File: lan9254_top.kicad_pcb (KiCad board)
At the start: 4 copper layers, 84 x 35 mm, 77 parts, among them J1 BEL_0845_2G1T_H5, SW1 SW_DIP_x08, U1 lan9254, U2 74LVC1G06, U3 74LVC1G06, U4 74LVC1G06, U5 PCA9306, U6 74LVC1G06, U8 24AA0x, X1 FNETHE025

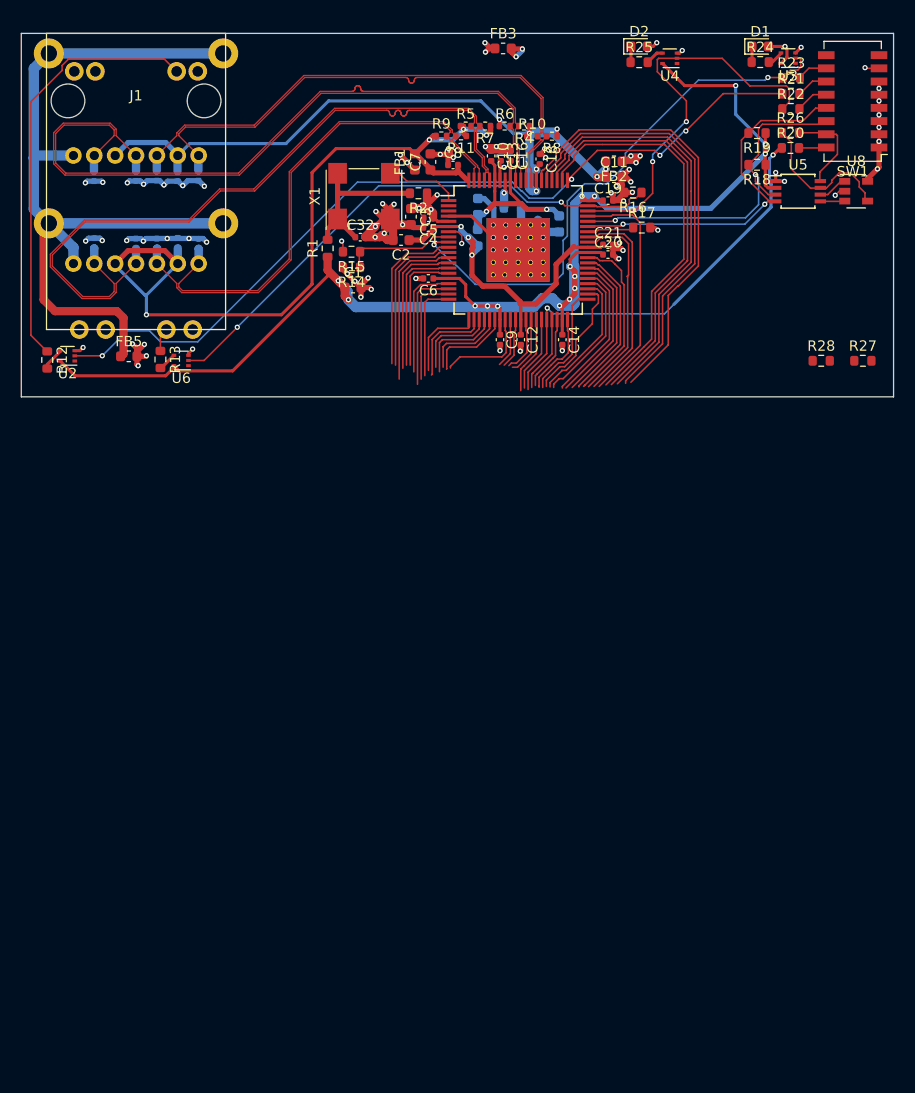
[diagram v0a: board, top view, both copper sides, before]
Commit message: added I/O connectors, JTAG (just in case) and more
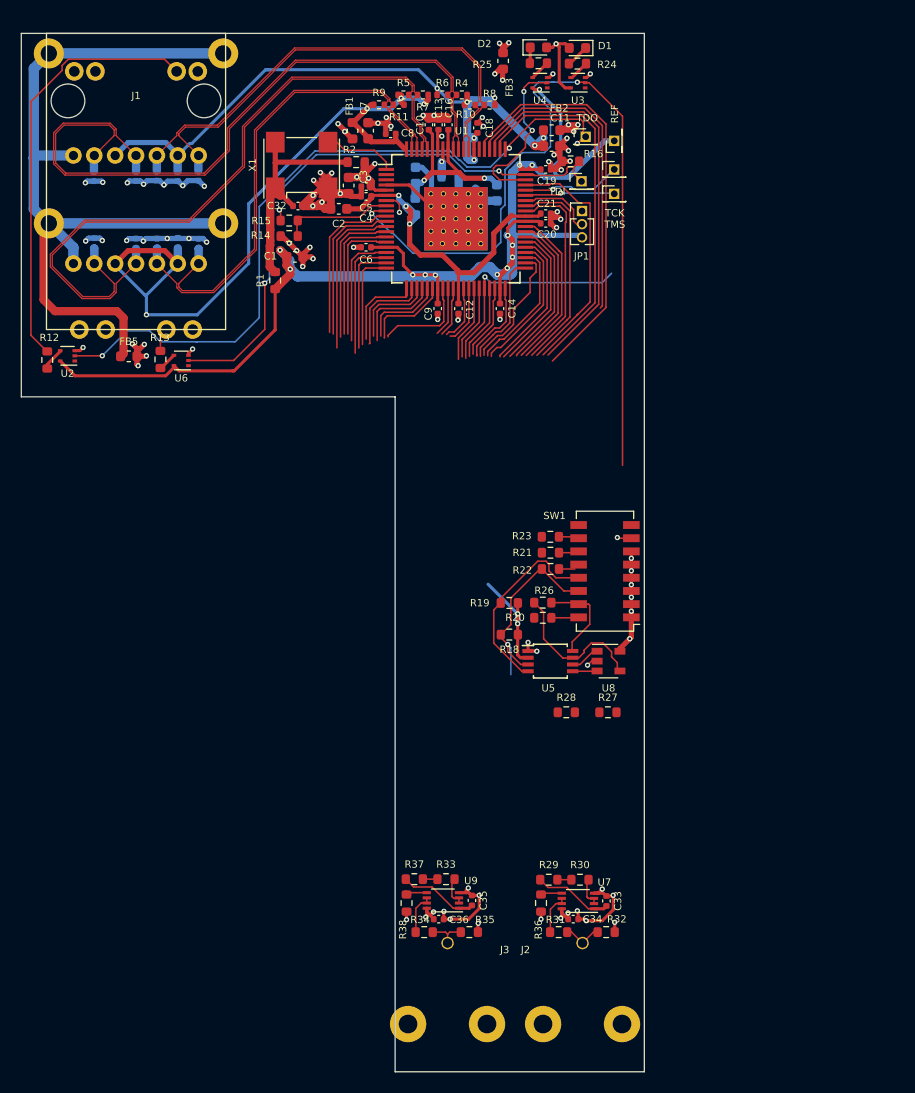
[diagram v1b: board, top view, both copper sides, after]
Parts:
- removed R17: 1k, Resistor_SMD:R_0603_1608Metric
- added C33: 100n, Capacitor_SMD:C_0402_1005Metric, F.Cu at (186.3, 123.5)
- added C34: 100n, Capacitor_SMD:C_0402_1005Metric, F.Cu at (183.2, 125.3)
- added C35: 100n, Capacitor_SMD:C_0402_1005Metric, F.Cu at (173.4, 123.5)
- added C36: 100n, Capacitor_SMD:C_0402_1005Metric, F.Cu at (170.2, 125.3)
- added J2: BNC, proj_footprints:BNC_Molex_0731713150, F.Cu at (184.1, 135.4)
- added J3: BNC, proj_footprints:BNC_Molex_0731713150, F.Cu at (171.1, 135.4)
- added JP1: Jumper_3_Bridged12, Connector_PinHeader_1.27mm:PinHeader_1x03_P1.27mm_Vertical, F.Cu at (184.0, 57.1)
- added R29: 100k, Resistor_SMD:R_0603_1608Metric, F.Cu at (180.8, 121.5)
- added R30: 100, Resistor_SMD:R_0603_1608Metric, F.Cu at (183.8, 121.5)
- added R31: 0, Resistor_SMD:R_0603_1608Metric, F.Cu at (181.8, 126.5)
- added R32: 100k, Resistor_SMD:R_0603_1608Metric, F.Cu at (186.3, 126.5)
- added R33: 100, Resistor_SMD:R_0603_1608Metric, F.Cu at (170.9, 121.5)
- added R34: 0, Resistor_SMD:R_0603_1608Metric, F.Cu at (168.8, 126.5)
- added R35: 100k, Resistor_SMD:R_0603_1608Metric, F.Cu at (173.2, 126.5)
- added R36: 2k2, Resistor_SMD:R_0603_1608Metric, F.Cu at (180.1, 123.8)
- added R37: 100k, Resistor_SMD:R_0603_1608Metric, F.Cu at (167.8, 121.5)
- added R38: 2k2, Resistor_SMD:R_0603_1608Metric, F.Cu at (167.1, 123.8)
- added TP1: TDO, Connector_PinHeader_1.27mm:PinHeader_1x01_P1.27mm_Vertical, F.Cu at (184.3, 50.0)
- added TP2: TDI, Connector_PinHeader_1.27mm:PinHeader_1x01_P1.27mm_Vertical, F.Cu at (183.9, 54.2)
- added TP3: TCK, Connector_PinHeader_1.27mm:PinHeader_1x01_P1.27mm_Vertical, F.Cu at (187.1, 53.1)
- added TP4: TMS, Connector_PinHeader_1.27mm:PinHeader_1x01_P1.27mm_Vertical, F.Cu at (187.1, 55.5)
- added TP5: REF, Connector_PinHeader_1.27mm:PinHeader_1x01_P1.27mm_Vertical, F.Cu at (187.1, 50.4)
- added U7: 74LVC2T45DC, Package_SO:VSSOP-8_2.3x2mm_P0.5mm, F.Cu at (183.6, 123.5)
- added U9: 74LVC2T45DC, Package_SO:VSSOP-8_2.3x2mm_P0.5mm, F.Cu at (170.6, 123.5)
- moved R18 51.2 mm to (177.0, 97.9)
- moved R20 51.2 mm to (180.2, 96.3)
- moved SW1 51.2 mm to (186.2, 91.8)
- moved U5 51.2 mm to (180.9, 100.5)
- moved U8 51.2 mm to (186.6, 100.5)
- moved R19 51.2 mm to (177.0, 94.8)
- moved R26 51.2 mm to (180.2, 94.8)
- moved R22 50.0 mm to (181.0, 91.6)
- moved R23 49.9 mm to (180.9, 88.5)
- moved R21 49.9 mm to (181.0, 90.0)
- moved R27 41.8 mm to (186.5, 105.4)
- moved R28 41.8 mm to (182.5, 105.4)
- moved U3 20.4 mm to (183.6, 44.8)
- moved D1 17.6 mm to (183.6, 41.4), turned to 180 degrees
- moved R24 17.6 mm to (183.6, 42.9)
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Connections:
- R22 pad 1: /lan9254/RUNLED -> /lan9254/EESCL
- U1 pad 58: /lan9254/RUNLED -> /lan9254/EESCL
- U4 pad 2: /lan9254/RUNLED -> /lan9254/EESCL
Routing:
- net /lan9254/FPGA_43: track 43.4 -> 0.00 mm
- net /lan9254/RUNLED: track 38.6 -> 0.00 mm, vias 2 -> 0
- net /lan9254/ERRLED: track 53.1 -> 78.8 mm
- net GND_lan9254: track 106.3 -> 126.7 mm, vias 64 -> 75
- net /lan9254/FPGA_23: track 41.1 -> 21.5 mm, vias 2 -> 1
- net /lan9254/LINKACT0: track 82.2 -> 70.7 mm, vias 4 -> 3
- net /lan9254/EESCL: track 35.0 -> 46.5 mm, vias 2 -> 4
- net /lan9254/FPGA_41: track 41.2 -> 31.3 mm
- net +1V8_lan9254: track 140.4 -> 149.9 mm
- net +3V3_lan9254: track 24.9 -> 33.5 mm, vias 15 -> 18
- net /lan9254/EESDA: track 36.2 -> 27.9 mm, vias 2 -> 1
- net Net-(C32-Pad1): track 16.3 -> 23.5 mm
- net /lan9254/VDD33TXRX2: track 76.5 -> 70.3 mm
- net /lan9254/rj45_ports/P0_TXD_P: track 51.8 -> 46.1 mm
- net /lan9254/rj45_ports/P0_TXD_N: track 51.7 -> 46.6 mm
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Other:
- board size 84 x 35 mm -> 60 x 100 mm
